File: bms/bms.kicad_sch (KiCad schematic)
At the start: 32 parts, among them J10 Conn_02x10_Odd_Even, J11 Conn_02x08_Odd_Even, J12 Conn_02x10_Odd_Even, J13 Conn_02x08_Odd_Even, J14 Conn_02x08_Odd_Even, J15 Conn_02x10_Odd_Even, J2 Conn_01x08_Socket, J3 Conn_01x06_Socket, J5 Conn_01x10_Socket, J6 Conn_01x08_Socket

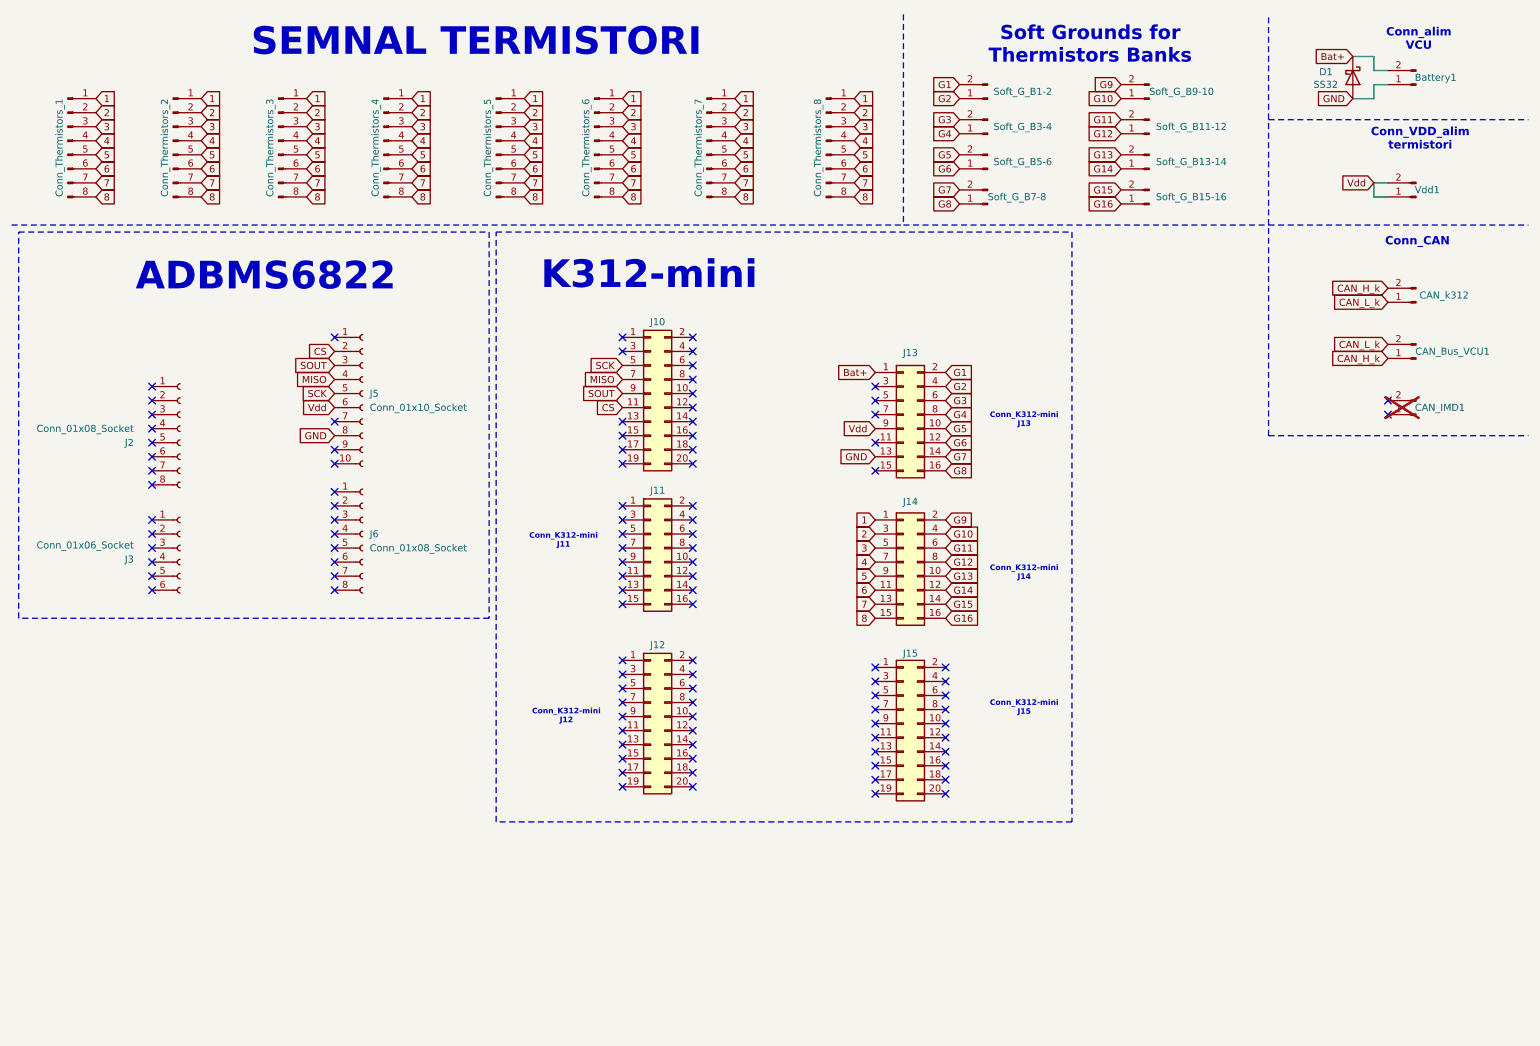
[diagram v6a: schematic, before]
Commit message: Check on layout+block diagram
4x mounting holes with GND connection - added;
PCB size small increaze
block diagram reshaped
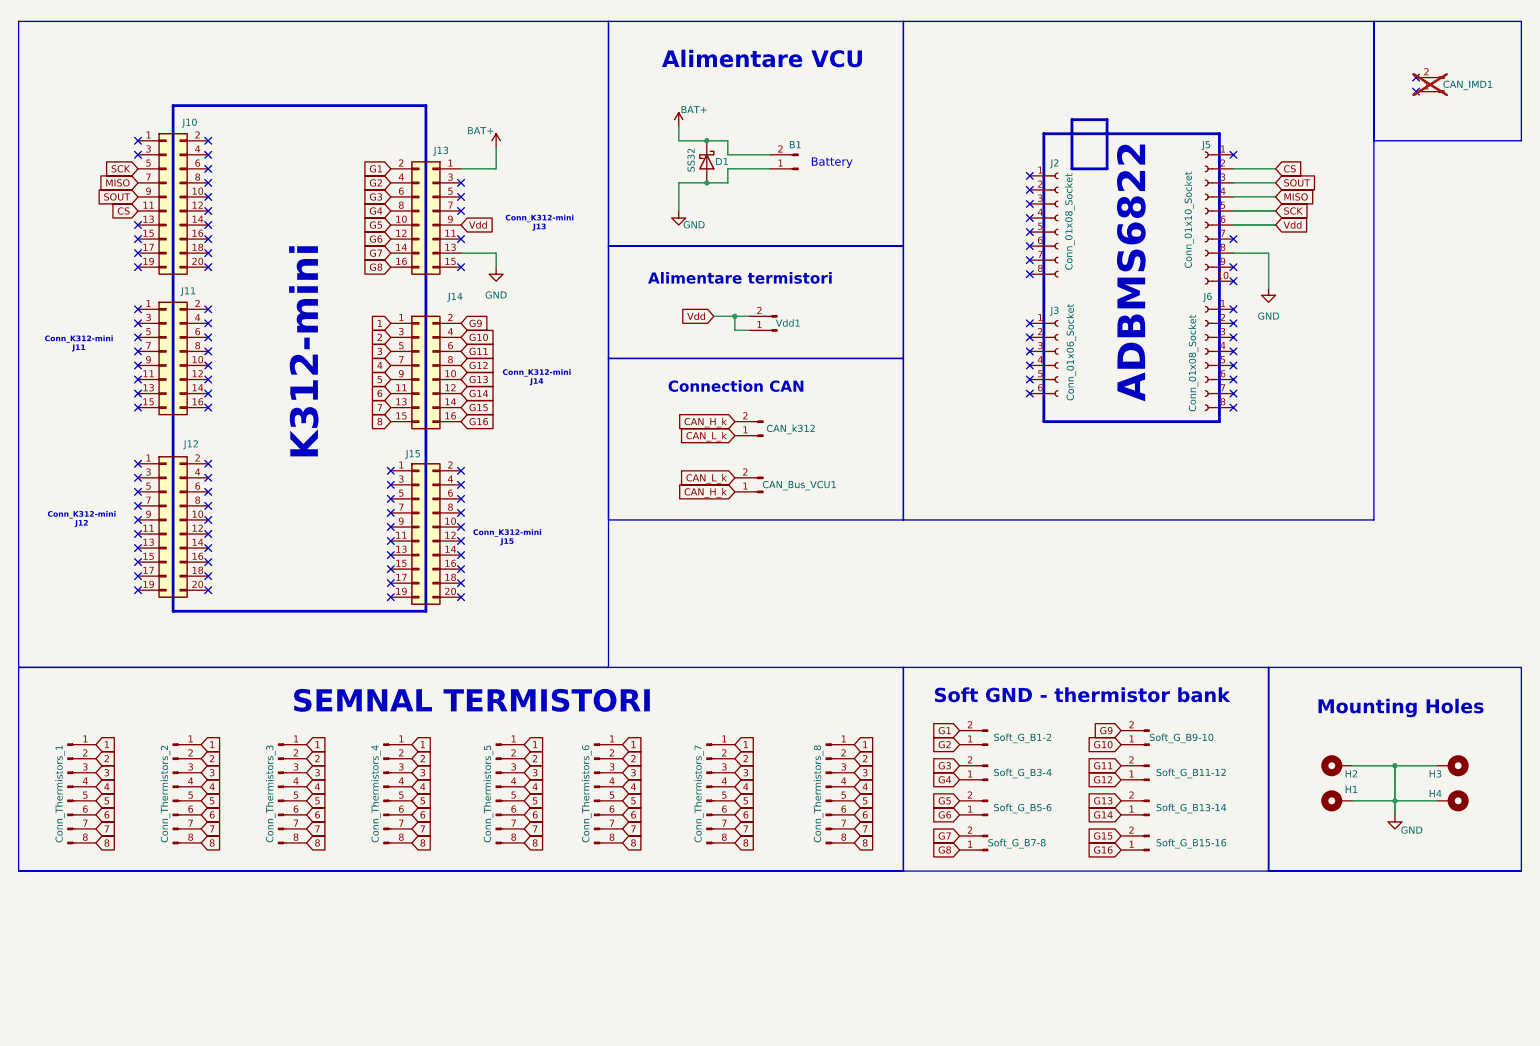
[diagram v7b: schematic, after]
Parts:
- added H1, H2, H3, H4: MountingHole_Pad, MountingHole:MountingHole_3.2mm_M3_ISO14580_Pad, symbol Mechanical:MountingHole_Pad
- renumbered Battery1 to B1
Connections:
- net GND: now also H1.1, H2.1, H3.1, H4.1
- net Bat+ renamed BAT+
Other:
- note added: "Alimentare VCU"
- note added: "Alimentare termistori"
- note added: "Battery"
- note added: "Connection CAN"
- note added: "Mounting Holes"
- note added: "Soft GND - thermistor bank"
- note removed: "Conn_CAN"
- note removed: "Conn_VDD_alim termistori"
- note removed: "Conn_alim VCU"
- note removed: "Soft Grounds for Thermistors Banks"
- moved on the sheet: B1, CAN_Bus_VCU1, CAN_IMD1, CAN_k312, Conn_Thermistors_1, Conn_Thermistors_2, Conn_Thermistors_3, Conn_Thermistors_4, Conn_Thermistors_5, Conn_Thermistors_6, Conn_Thermistors_7, Conn_Thermistors_8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

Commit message: PCB modified - lange update
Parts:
- added C1: 1uF, Capacitor_SMD:C_0805_2012Metric_Pad1.18x1.45mm_HandSolder, symbol Device:C_Small
- added C2: 2.2uF, Capacitor_SMD:C_0805_2012Metric_Pad1.18x1.45mm_HandSolder, symbol Device:C_Small
- added U1: TLV76150DCY, Package_TO_SOT_SMD:SOT-223-3_TabPin2, symbol Regulator_Linear:TLV76150DCY
- D1: footprint Diode_SMD:D_SMB -> Diode_THT:D_A-405_P7.62mm_Horizontal
- renumbered Vdd1 to 5Vdd1, J5 to J3, J2 to J4, J6 to J5, J3 to J6
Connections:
- net BAT+: now also B1.1 (Pin_1), C1.1, U1.3 (VI); no longer B1.2 (Pin_2)
- net G10: now also J12.18 (Pin_18); no longer J14.4 (Pin_4)
- net G11: now also J12.16 (Pin_16); no longer J14.6 (Pin_6)
- net G12: now also J12.14 (Pin_14); no longer J14.8 (Pin_8)
- net G13: now also J12.8 (Pin_8); no longer J14.10 (Pin_10)
- net G14: now also J12.6 (Pin_6); no longer J14.12 (Pin_12)
- net G15: now also J12.4 (Pin_4); no longer J14.14 (Pin_14)
- net G16: now also J12.2 (Pin_2); no longer J14.16 (Pin_16)
- net GND: now also B1.2 (Pin_2), C1.2, C2.2, U1.1 (GND); no longer B1.1 (Pin_1)
- net G09: now reaches J12.20 (Pin_20)
- net G09: now also Soft_G_B9-10.2 (Pin_2)
- net G06: now reaches J10.10 (Pin_10)
- net G06: now also Soft_G_B5-6.1 (Pin_1)
- net G05: now reaches J10.12 (Pin_12)
- net G05: now also Soft_G_B5-6.2 (Pin_2)
- net G04: now reaches J10.14 (Pin_14)
- net G04: now also Soft_G_B3-4.1 (Pin_1)
- net G03: now reaches J10.16 (Pin_16)
- net G03: now also Soft_G_B3-4.2 (Pin_2)
- net G02: now reaches J10.18 (Pin_18)
- net G02: now also Soft_G_B1-2.1 (Pin_1)
- net G01: now reaches J10.20 (Pin_20)
- net G01: now also Soft_G_B1-2.2 (Pin_2)
- net G08: now reaches J10.6 (Pin_6)
- net G08: now also Soft_G_B7-8.1 (Pin_1)
- net G07: now reaches J10.8 (Pin_8)
- net G07: now also Soft_G_B7-8.2 (Pin_2)
- net G1: no longer names the net of J13.2 (Pin_2)
- net G1: no longer Soft_G_B1-2.2 (Pin_2)
- net G2: no longer names the net of J13.4 (Pin_4)
- net G2: no longer Soft_G_B1-2.1 (Pin_1)
- net G3: no longer names the net of J13.6 (Pin_6)
- net G3: no longer Soft_G_B3-4.2 (Pin_2)
- net G4: no longer names the net of J13.8 (Pin_8)
- net G4: no longer Soft_G_B3-4.1 (Pin_1)
- net G5: no longer names the net of J13.10 (Pin_10)
- net G5: no longer Soft_G_B5-6.2 (Pin_2)
- net G6: no longer names the net of J13.12 (Pin_12)
- net G6: no longer Soft_G_B5-6.1 (Pin_1)
- net G7: no longer names the net of J13.14 (Pin_14)
- net G7: no longer Soft_G_B7-8.2 (Pin_2)
- net G8: no longer names the net of J13.16 (Pin_16)
- net G8: no longer Soft_G_B7-8.1 (Pin_1)
- net G9: no longer names the net of J14.2 (Pin_2)
- net G9: no longer Soft_G_B9-10.2 (Pin_2)
- net Vdd renamed 5V
- net 5V: no longer J13.9 (Pin_9)
- new net 5V1: C2.1, U1.2 (VO)
- no-connect marks 105 -> 106
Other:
- moved on the sheet: B1, D1, J10, J12, J14, Soft_G_B1-2, Soft_G_B11-12, Soft_G_B13-14, Soft_G_B15-16, Soft_G_B3-4, Soft_G_B5-6, Soft_G_B7-8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
